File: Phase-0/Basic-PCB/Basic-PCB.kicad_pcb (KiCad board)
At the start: 2 copper layers, 68.6 x 90.8 mm, 28 parts, among them J1 Flexor Digitorum Superficialis, J2 Flexor Carpi Radialis, J3 output, U1 LM358, U2 LM358, U3 LM358

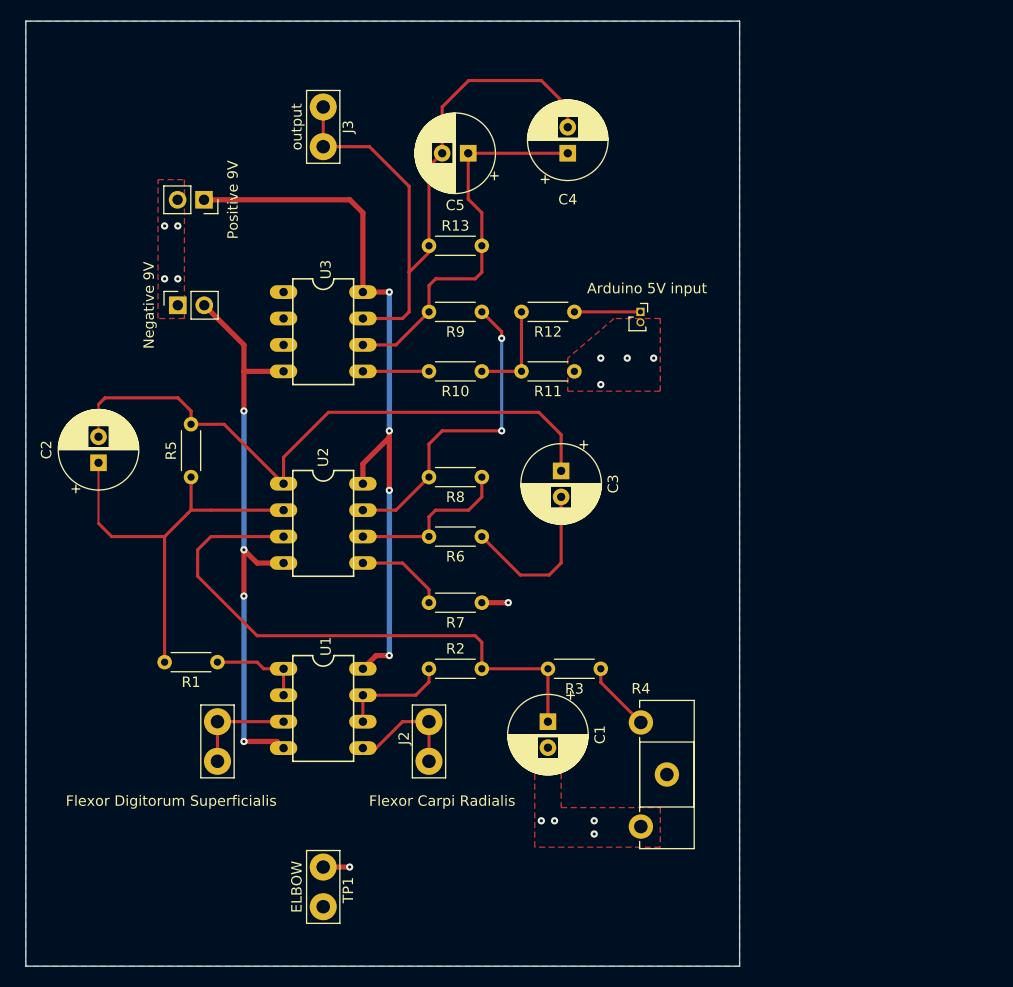
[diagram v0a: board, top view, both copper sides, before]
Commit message: Improved Phase 0 PCB
Made slightly more compact PCB and include op amp models
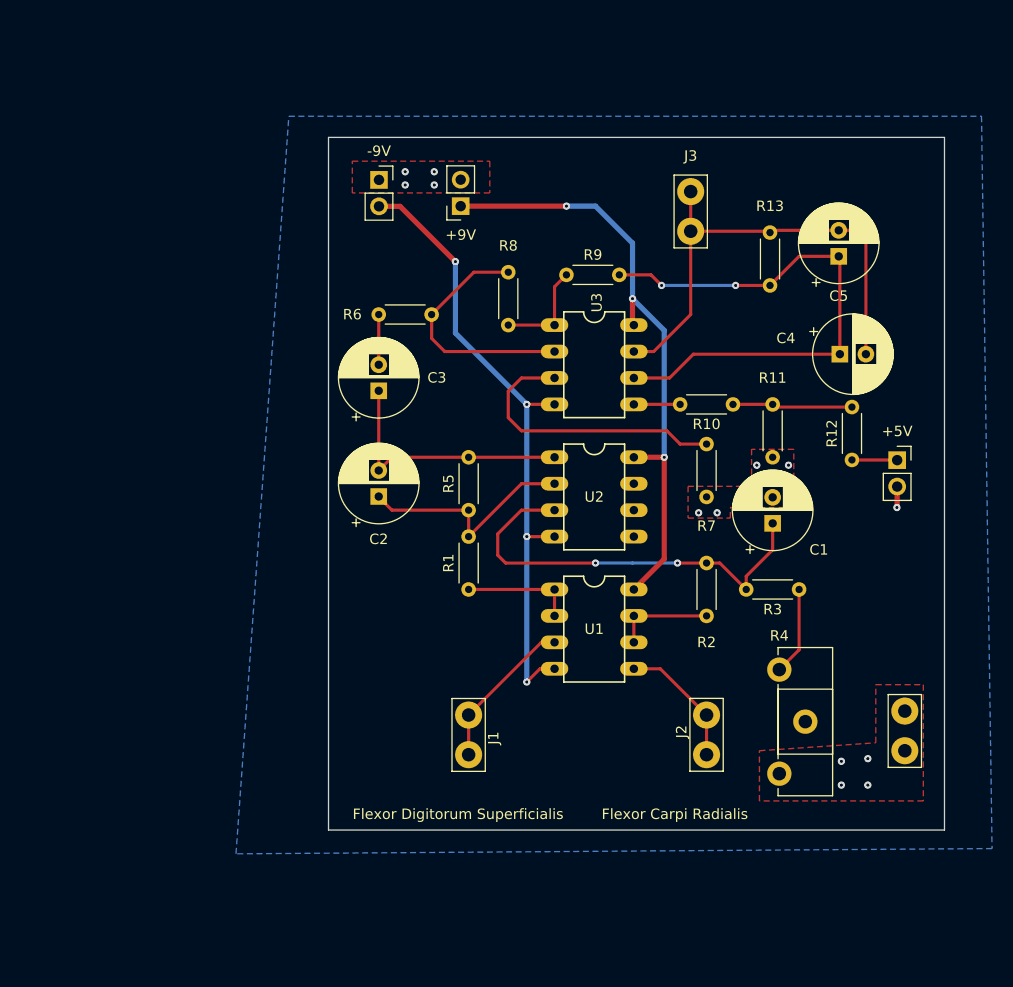
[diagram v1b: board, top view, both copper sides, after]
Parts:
- removed Arduino 5V input: Conn_01x02, Connector_PinSocket_1.00mm:PinSocket_1x02_P1.00mm_Vertical
- removed Negative 9V: Battery, Connector_PinSocket_2.54mm:PinSocket_1x02_P2.54mm_Vertical
- removed Positive 9V: Battery, Connector_PinSocket_2.54mm:PinSocket_1x02_P2.54mm_Vertical
- added +5V: Conn_01x02, Connector_PinSocket_2.54mm:PinSocket_1x02_P2.54mm_Vertical, F.Cu at (192.3, 93.0)
- added +9V: Battery, Connector_PinSocket_2.54mm:PinSocket_1x02_P2.54mm_Vertical, F.Cu at (150.4, 68.6)
- added -9V: Battery, Connector_PinSocket_2.54mm:PinSocket_1x02_P2.54mm_Vertical, F.Cu at (142.5, 66.1)
- moved TP1 57.9 mm to (193.0, 120.9)
- moved C5 37.0 mm to (186.7, 73.4), turned to 90 degrees
- moved J3 36.2 mm to (172.5, 71.0)
- moved R13 32.8 mm to (180.1, 71.1), turned to -90 degrees
- moved C4 32.5 mm to (186.8, 82.8), turned to 0 degrees
- moved R12 30.2 mm to (188.0, 93.0), turned to 90 degrees
- moved C1 28.8 mm to (180.3, 99.1), turned to 90 degrees
- moved R2 27.1 mm to (174.0, 108.0), turned to 90 degrees
- moved U1 27.1 mm to (163.2, 109.2)
- moved C2 27.1 mm to (142.5, 96.5)
- moved R5 26.9 mm to (151.1, 97.8)
- moved J2 26.7 mm to (174.0, 117.5)
- moved U3 26.2 mm to (163.2, 83.8)
- moved U2 26.2 mm to (163.2, 96.5)
- moved R1 25.1 mm to (151.1, 105.4), turned to 90 degrees
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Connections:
- R6 pad 2: Net-(U2B--) -> Net-(U3A--)
- R7 pad 2: Net-(U2B-+) -> Net-(U3A-+)
- R8 pad 1: Net-(U2B--) -> Net-(U3A--)
- U2 pad 5: Net-(U2B-+) -> (no net)
- U2 pad 6: Net-(U2B--) -> (no net)
- U2 pad 7: Net-(R8-Pad2) -> (no net)
- U3 pad 1: (no net) -> Net-(R8-Pad2)
- U3 pad 2: (no net) -> Net-(U3A--)
- U3 pad 3: (no net) -> Net-(U3A-+)
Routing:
- net Net-(C2-Pad2): track 60.7 -> 25.1 mm
- net Net-(U3A-+): track 0.00 -> 27.6 mm
- net Net-(U3A--): track 0.00 -> 23.7 mm
- net Net-(R8-Pad2): track 30.6 -> 9.74 mm, vias 2 -> 0
- net Net-(U2A--): track 40.4 -> 22.1 mm
- net Net-(U2B--): track 16.0 -> 0.00 mm
- net /A0: track 63.7 -> 48.2 mm
- net Net-(U3B--): track 37.3 -> 52.8 mm, vias 0 -> 2
- net Net-(U2A-+): track 55.2 -> 41.1 mm, vias 0 -> 2
- net Net-(C3-Pad2): track 16.0 -> 4.83 mm
- net +9V: track 69.4 -> 59.2 mm, vias 4 -> 3
- net Net-(U2B-+): track 8.67 -> 0.00 mm
- net -9V: track 55.7 -> 61.3 mm
- net Net-(J1-Pin_1): track 10.2 -> 15.0 mm
- net GND: track 5.08 -> 2.02 mm, vias 14 -> 13
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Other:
- board size 68.6 x 90.8 mm -> 59.2 x 66.5 mm

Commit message: Changed footprints for battery terminals
Changed footprints for battery terminals to ones found in a Makerspace nearby
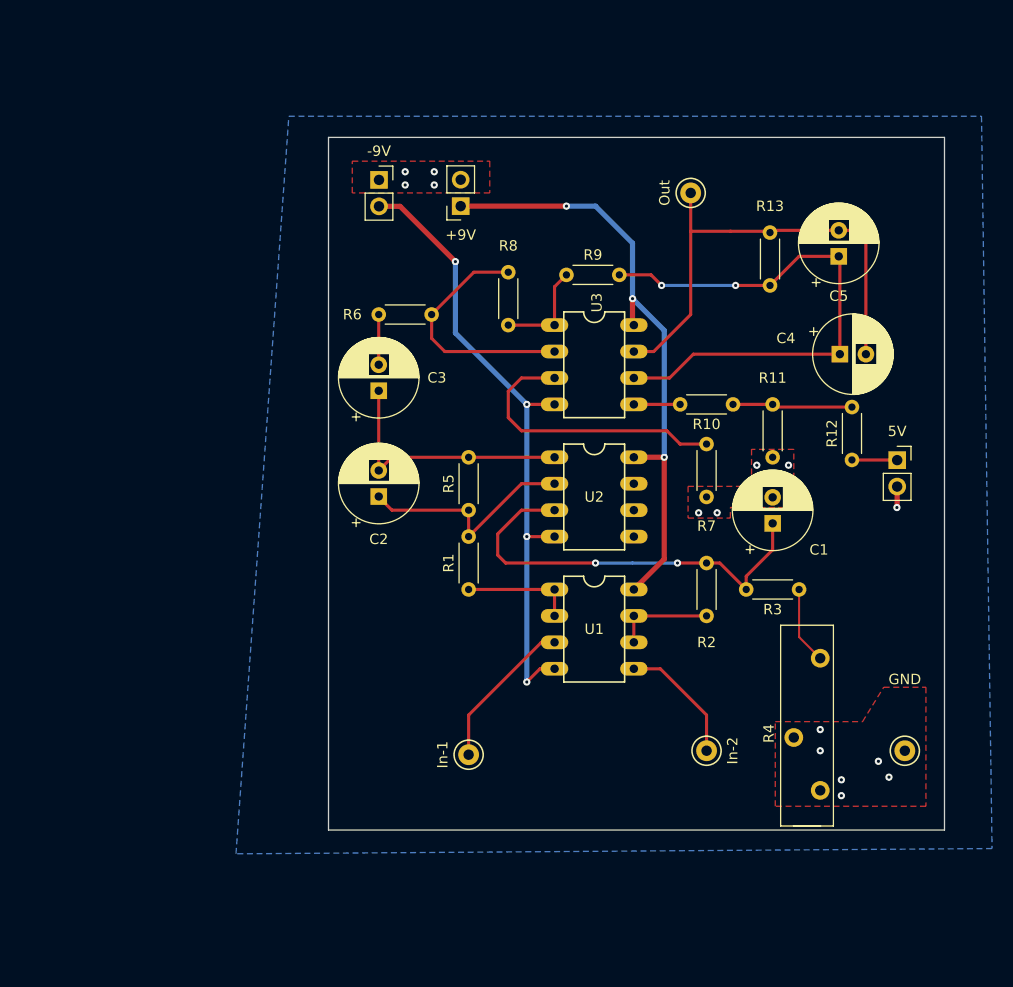
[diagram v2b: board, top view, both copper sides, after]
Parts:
- GND: renamed from TP1; footprint TestPoint:TestPoint_Bridge_Pitch3.81mm_Drill1.3mm -> TestPoint:TestPoint_Keystone_5000-5004_Miniature
- In-1: renamed from J1; value Flexor Digitorum Superficialis -> In1; footprint TestPoint:TestPoint_Bridge_Pitch3.81mm_Drill1.3mm -> TestPoint:TestPoint_Keystone_5000-5004_Miniature
- In-2: renamed from J2; value Flexor Carpi Radialis -> In2; footprint TestPoint:TestPoint_Bridge_Pitch3.81mm_Drill1.3mm -> TestPoint:TestPoint_Keystone_5000-5004_Miniature
- Out: renamed from J3; footprint TestPoint:TestPoint_Bridge_Pitch3.81mm_Drill1.3mm -> TestPoint:TestPoint_Keystone_5000-5004_Miniature
- R4: footprint Potentiometer_THT:Potentiometer_ACP_CA14-H2,5_Horizontal -> Potentiometer_THT:Potentiometer_Bourns_3006P_Horizontal
- moved R4 4.08 mm to (184.9, 112.0), turned to 90 degrees
- moved Out 3.68 mm to (172.5, 67.3)
- moved In-2 3.43 mm to (174.0, 120.9)
- renumbered +5V to 5V
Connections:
- R4 pad 2: unconnected-(R4-Pad2) -> GND
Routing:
- net Net-(R3-Pad1): track 8.49 -> 7.45 mm
- net GND: vias 13 -> 15
